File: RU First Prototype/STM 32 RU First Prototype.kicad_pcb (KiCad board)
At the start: 4 copper layers, 91 parts, among them J1 Conn_01x02, J10 Conn_01x02_Pin, J11 Conn_01x02_Pin, J12 1776113-2, J2 USB_C_Receptacle, J3 Conn_01x02_Pin, J4 Conn_01x04, J5 Conn_01x02_Pin, J7 1776113-2, J9 Conn_01x02_Pin, Q1 SISA96DN-T1, Q3 SISA96DN-T1, SW1 SW_SPDT, U1 STM32F412RGTx, U2 AMS1117-3.3, U3 MS5611, U4 KX134-1211, U5 W25Q16JVSS, U6 TCAN330, U7 TCAN330, Y1 Crystal_8Mhz

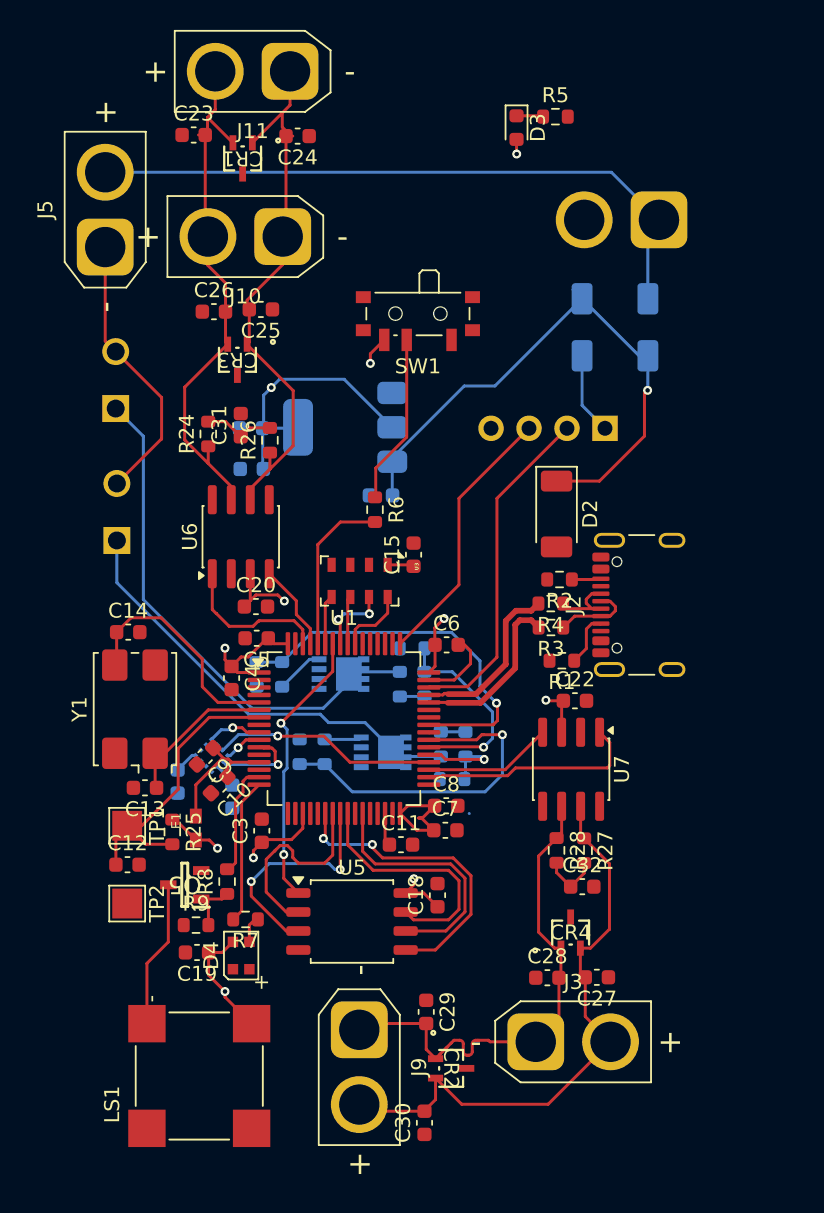
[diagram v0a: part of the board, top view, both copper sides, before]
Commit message: Edge cuts to start
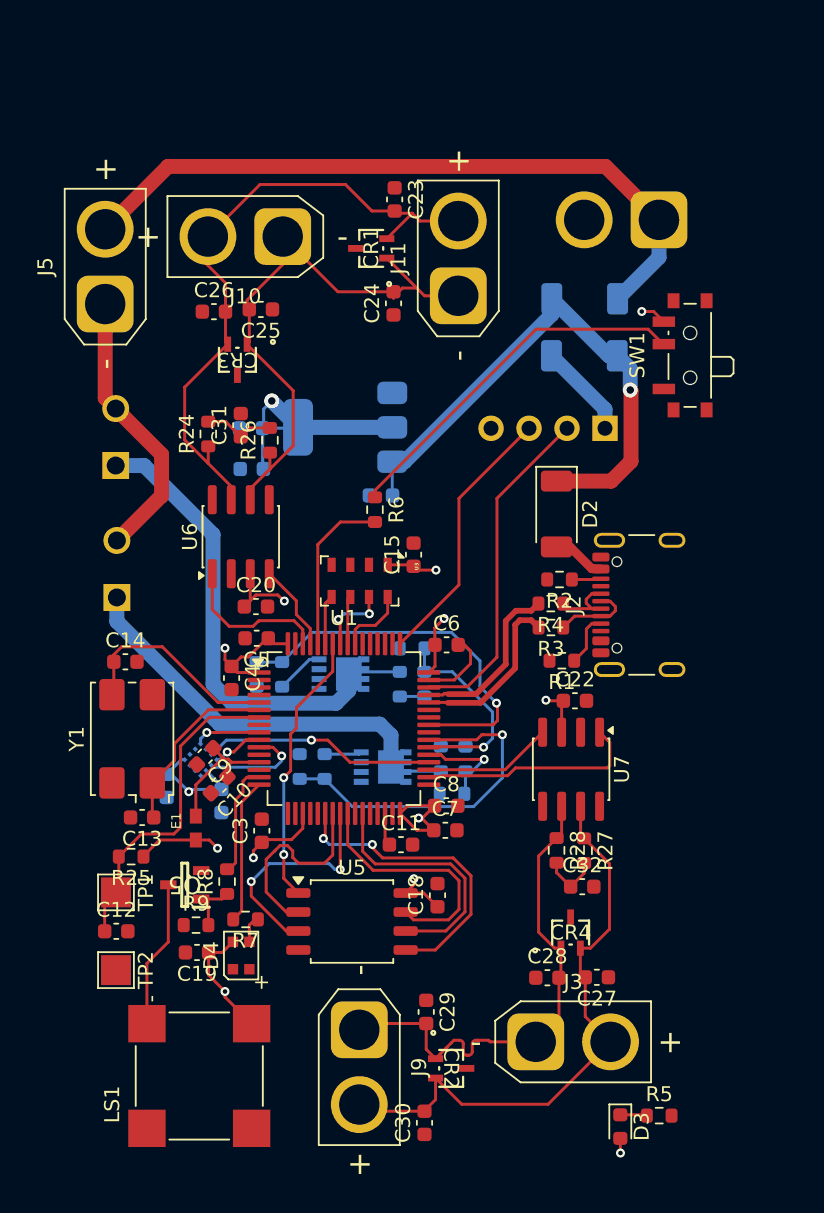
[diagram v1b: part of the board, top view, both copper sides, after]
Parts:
- moved R5 67.2 mm to (142.5, 125.7)
- moved D3 67.2 mm to (139.9, 126.4)
- moved J11 18.8 mm to (129.0, 70.9), turned to 90 degrees
- moved SW1 18.0 mm to (144.2, 74.8), turned to 90 degrees
- moved C23 14.1 mm to (124.8, 64.4), turned to -90 degrees
- moved C24 12.9 mm to (124.7, 71.4), turned to 90 degrees
- moved CR1 10.5 mm to (123.2, 67.7), turned to 90 degrees
- moved C12 4.52 mm to (106.2, 113.4)
- moved TP1 4.52 mm to (106.1, 110.8)
- moved TP2 4.52 mm to (106.1, 116.0)
- moved J12 3.81 mm to (106.1, 80.3)
- moved J5 3.81 mm to (105.4, 71.4)
- moved J7 3.81 mm to (106.2, 89.1)
- moved R25 3.21 mm to (107.1, 108.4), turned to 180 degrees
- moved D5 2.05 mm to (137.4, 74.9)
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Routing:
- net Net-(SW1-B): track 11.4 -> 24.7 mm
- net /CAN_H: track 35.9 -> 43.7 mm
- net +3V3: track 75.4 -> 81.1 mm, vias 11 -> 14
- net /V_2S: track 43.9 -> 47.7 mm
- net /V_USB: track 0.42 -> 4.00 mm
- net /CAN_L: track 36.8 -> 39.2 mm
- net /OSC_OUT: track 10.5 -> 12.8 mm
- net /V_IN: track 39.9 -> 38.0 mm
- net /NRST: track 20.0 -> 22.0 mm
- net /V_MAIN: track 35.0 -> 33.5 mm
- net /OSC_IN: track 15.6 -> 14.2 mm
- net /KX_SDI: track 6.12 -> 7.34 mm
- net /KX_SDO: track 2.54 -> 3.39 mm
- net /SW_VCC: track 5.48 -> 6.33 mm
- net /KX_CS: track 3.64 -> 4.43 mm
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
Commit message: Added fill zones and all
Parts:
- added REF**: MountingHole_3.2mm_M3, MountingHole:MountingHole_3.2mm_M3, F.Cu at (151.2, 61.7)
- added REF**: MountingHole_3.2mm_M3, MountingHole:MountingHole_3.2mm_M3, F.Cu at (98.8, 61.6)
- added REF**: MountingHole_3.2mm_M3, MountingHole:MountingHole_3.2mm_M3, F.Cu at (98.7, 127.4)
- added REF**: MountingHole_3.2mm_M3, MountingHole:MountingHole_3.2mm_M3, F.Cu at (151.2, 127.4)
- moved R20 2.92 mm to (128.4, 96.0), turned to 90 degrees
- moved R11 1.73 mm to (115.5, 94.5), turned to -90 degrees
- moved R14 1.72 mm to (118.4, 104.0), turned to 90 degrees
- moved C22 1.54 mm to (135.3, 97.9)
- moved C12 1.28 mm to (107.4, 113.2)
- moved R2 1.20 mm to (134.6, 89.7)
- moved R19 1.08 mm to (126.8, 97.9)
- moved C5 1.07 mm to (114.5, 94.0)
- moved C10 1.05 mm to (113.6, 104.5), turned to -90 degrees
- moved C4 0.99 mm to (112.9, 96.4), turned to 135 degrees
- moved U5 0.94 mm to (121.9, 113.6)
- moved R23 0.83 mm to (128.1, 104.8)
- moved C32 0.82 mm to (136.5, 110.5)
- moved C13 0.79 mm to (107.1, 105.6)
- moved R18 0.77 mm to (125.1, 97.6)
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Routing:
- net GND: track 6.88 -> 19.4 mm, vias 0 -> 40
- net /V_USB: track 4.00 -> 12.0 mm
- net +3V3: track 81.1 -> 76.5 mm
- net /Main: track 26.0 -> 29.4 mm
- net /PC7: track 13.5 -> 10.6 mm
- net /ALT_CS: track 3.30 -> 5.45 mm
- net /FLASH_IO0: track 20.7 -> 22.3 mm
- net /FLASH_CLK: track 16.9 -> 18.5 mm
- net Net-(J2-CC2): track 1.96 -> 3.23 mm
- net /FLASH_CS: track 18.4 -> 19.7 mm
- net /FLASH_IO3: track 16.5 -> 17.7 mm
- net /FLASH_IO2: track 15.5 -> 16.5 mm
- net /PC6: track 6.91 -> 7.87 mm
- net /FLASH_IO1: track 13.6 -> 14.5 mm
- net /OSC_IN: track 14.2 -> 15.0 mm
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- added copper zone on In2.Cu, net +3V3
- added copper zone on B.Cu, net GND
- added copper zone on F.Cu, net GND
- added copper zone on In1.Cu, net GND
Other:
- board outline added: 60.8 x 74.2 mm

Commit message: Made some changes
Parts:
- added G***: LOGO, RT_Graphics:RT_logo, F.Cu at (133.0, 59.0)
- added G***: LOGO, RT_Graphics:Ember_logo, F.Cu at (121.5, 76.5)
- added REF**: KiCad-Logo2_5mm_SilkScreen, Symbol:KiCad-Logo2_5mm_SilkScreen, F.Cu at (115.5, 58.0)
- moved REF** 9.42 mm to (143.0, 132.0)
- moved REF** 9.20 mm to (143.0, 57.5)
- moved R5 8.82 mm to (135.8, 131.5)
- moved REF** 7.81 mm to (105.0, 132.0)
- moved REF** 7.41 mm to (105.0, 57.5)
- moved D3 4.82 mm to (135.8, 129.0), turned to 0 degrees
- moved R11 1.81 mm to (115.0, 96.2)
- moved R14 1.73 mm to (118.5, 102.3), turned to -90 degrees
- moved C17 1.71 mm to (108.5, 105.0)
- moved R20 1.67 mm to (128.4, 97.7), turned to -90 degrees
- moved C16 0.90 mm to (114.0, 105.0)
- moved R22 0.82 mm to (129.0, 102.5)
- moved C1 0.79 mm to (123.8, 85.0)
- moved R21 0.75 mm to (127.4, 102.4)
- moved R19 0.28 mm to (126.7, 97.6)
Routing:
- net /V_2S: track 47.7 -> 52.2 mm
- net +3V3: track 76.5 -> 79.8 mm, vias 14 -> 19
- net /Main: track 29.4 -> 31.4 mm
- net /V_IN: track 38.0 -> 39.8 mm
- net GND: track 19.4 -> 20.8 mm, vias 40 -> 44
- net /V_DROGUE: track 28.5 -> 27.3 mm
- net Net-(D3-K): track 1.80 -> 2.50 mm
- net /SW_VCC: track 6.33 -> 6.87 mm
- added copper zone on B.Cu, net +3V3
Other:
- board size 60.8 x 74.2 mm -> 45 x 81.5 mm
- board text added: "Aug 2026"
- board text added: "EMBER"
- board text added: "RU V1 R1"

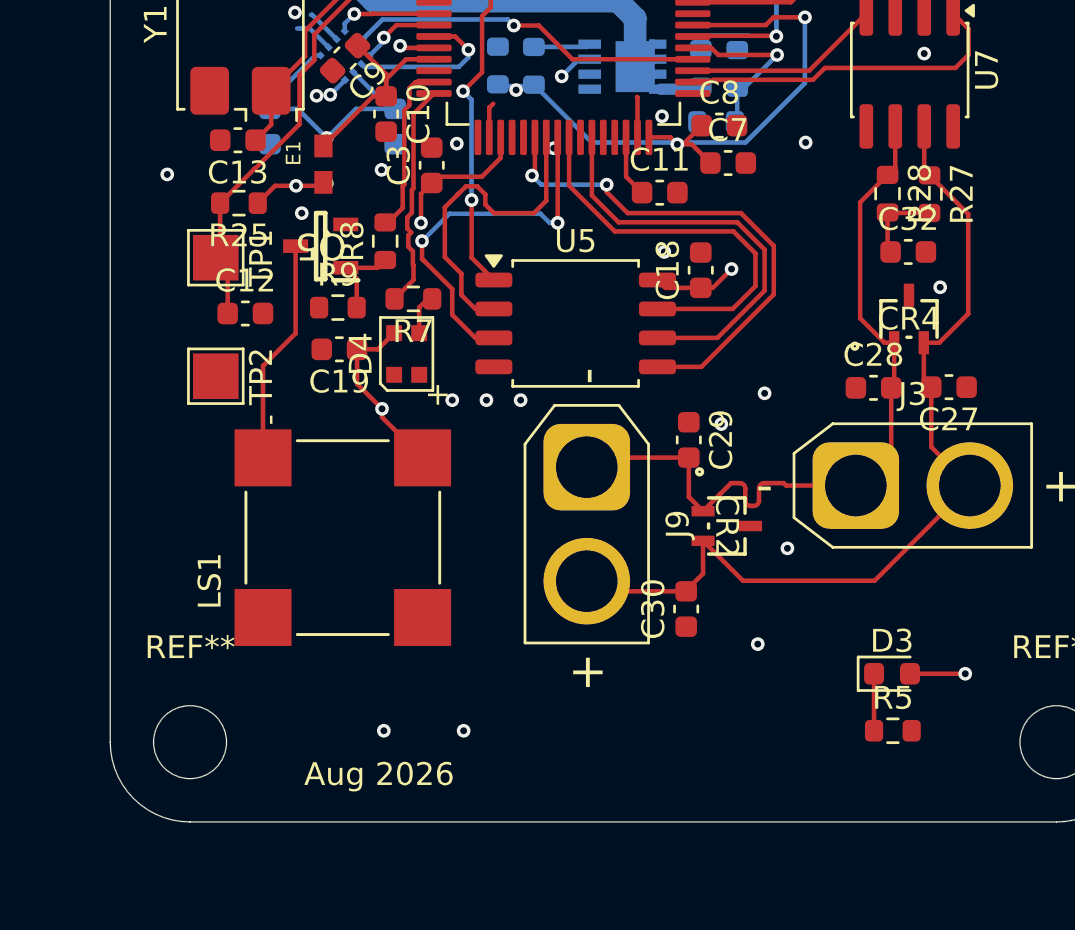
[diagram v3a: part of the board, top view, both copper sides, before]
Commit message: made some changes to routings
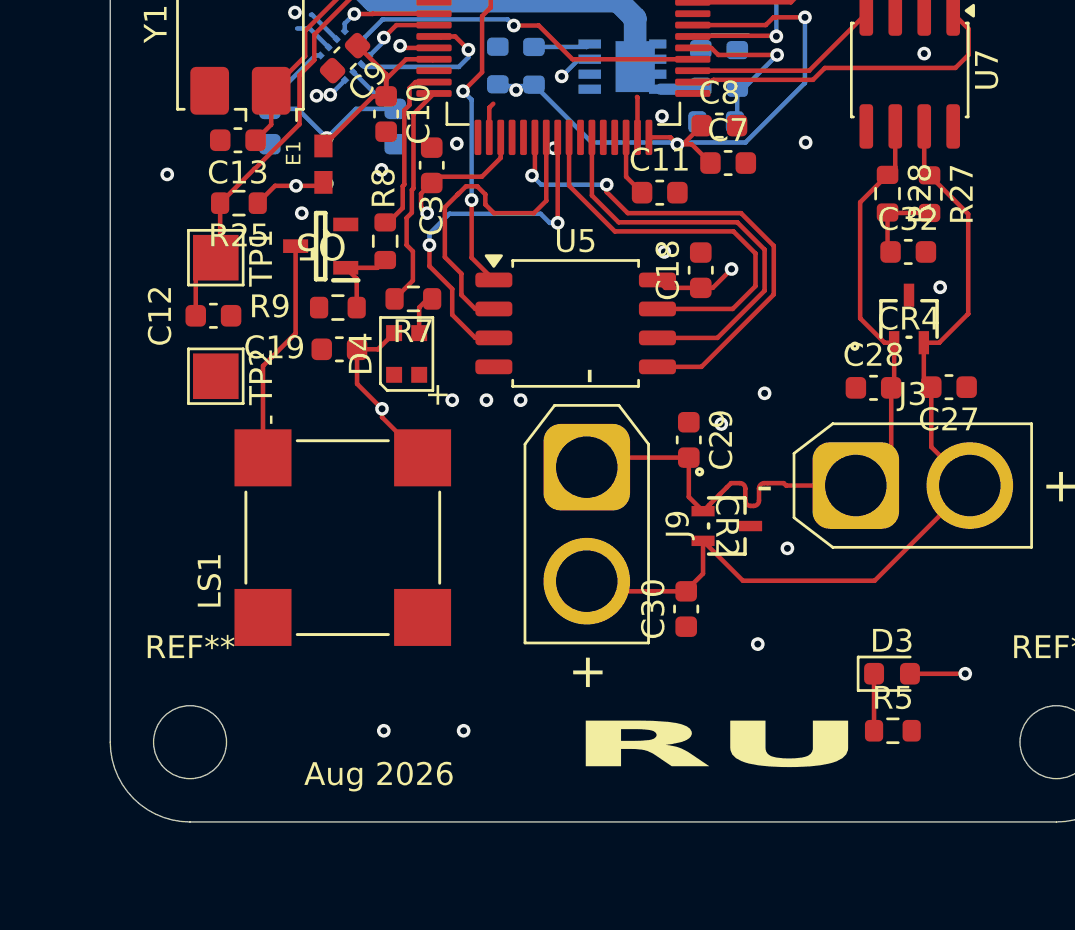
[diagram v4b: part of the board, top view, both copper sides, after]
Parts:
- moved C12 1.40 mm to (106.0, 113.3)
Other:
- board text added: "RU"
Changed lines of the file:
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@@
 		(tags "resistor")
 		(property "Reference" "R9"
-			(at 0 -1.43 0)
+			(at -2.985 -0.04 0)
 			(layer "F.SilkS")
 			(effects
@@
 		(tags "capacitor")
 		(property "Reference" "C19"
-			(at 0 -1.43 0)
+			(at 2.85 0.07 0)
 			(layer "F.SilkS")
 			(effects
@@
 		)
 		(property "Value" "STM32F412RGTx"
-			(at -8.595 7.545 0)
+			(at 0 0 0)
 			(layer "F.Fab")
 			(effects
@@
 	(footprint "Capacitor_SMD:C_0603_1608Metric"
 		(layer "F.Cu")
-		(at 107.425 113.2)
+		(at 106.025 113.3)
 		(descr "Capacitor SMD 0603 (1608 Metric), square (rectangular) end terminal, IPC-7351 nominal, (Body size source: IPC-SM-782 page 76, https://www.pcb-3d.com/wordpress/wp-content/uploads/ipc-sm-782a_amendment_1_and_2.pdf), generated with kicad-footprint-generator")
 		(tags "capacitor")
 		(property "Reference" "C12"
-			(at 0 -1.43 0)
+			(at -2.325 0 90)
 			(layer "F.SilkS")
 			(effects
@@
 		(tags "capacitor")
 		(property "Reference" "C3"
-			(at 0 -1.43 90)
+			(at -2.2 0 90)
 			(layer "F.SilkS")
 			(effects
@@
 		(tags "resistor")
 		(property "Reference" "R8"
-			(at 0 -1.43 90)
+			(at 2.33 -0.06 90)
 			(layer "F.SilkS")
 			(effects
@@
 		)
 	)
+	(gr_text "RU"
+		(at 121.6 133.3 0)
+		(layer "F.SilkS")
+		(effects
+			(font
+				(face "OCR A Extended")
+				(size 2 6)
+				(thickness 0.5)
+				(bold yes)
+			)
+			(justify left bottom)
+		)
+		(render_cache "RU" 0
+			(polygon
+				(pts
+					(xy 125.175013 131.150416) (xy 125.417517 131.184286) (xy 125.638799 131.241995) (xy 125.81162 131.315835)
+					(xy 125.913162 131.396908) (xy 125.947644 131.487948) (xy 125.947644 131.618374) (xy 125.913187 131.71032)
+					(xy 125.81207 131.791612) (xy 125.640631 131.865059) (xy 125.420782 131.92223) (xy 125.177746 131.955922)
+					(xy 124.90314 131.967397) (xy 124.485118 131.967397) (xy 125.884263 132.769612) (xy 125.93548 132.806879)
+					(xy 125.951674 132.842763) (xy 125.924444 132.887235) (xy 125.841399 132.925439) (xy 125.722749 132.951529)
+					(xy 125.591538 132.96) (xy 125.461472 132.953089) (xy 125.356398 132.932565) (xy 125.26987 132.896741)
+					(xy 123.65457 131.967397) (xy 123.176831 131.967397) (xy 123.176831 132.841053) (xy 123.149855 132.886968)
+					(xy 123.068754 132.925439) (xy 122.950499 132.951386) (xy 122.812665 132.96) (xy 122.675206 132.951337)
+					(xy 122.56024 132.925439) (xy 122.482542 132.887235) (xy 122.456559 132.841542) (xy 122.456559 131.732923)
+					(xy 123.168771 131.732923) (xy 124.902773 131.732923) (xy 125.031406 131.724912) (xy 125.138346 131.70105)
+					(xy 125.211121 131.665636) (xy 125.235432 131.623258) (xy 125.235432 131.490879) (xy 125.211109 131.448523)
+					(xy 125.138346 131.41321) (xy 125.031378 131.389252) (xy 124.902773 131.381214) (xy 123.168771 131.381214)
+					(xy 123.168771 131.732923) (xy 122.456559 131.732923) (xy 122.456559 131.138925) (xy 124.90314 131.138925)
+				)
+			)
+			(polygon
+				(pts
+					(xy 127.510554 132.61232) (xy 127.510554 131.260191) (xy 127.536886 131.214324) (xy 127.616434 131.174951)
+					(xy 127.732943 131.147812) (xy 127.86666 131.138925) (xy 128.000484 131.147659) (xy 128.116521 131.174218)
+					(xy 128.196491 131.212788) (xy 128.222766 131.25726) (xy 128.222766 132.609877) (xy 128.247102 132.65015)
+					(xy 128.321685 132.685471) (xy 128.429967 132.709704) (xy 128.555425 132.717711) (xy 129.965195 132.717711)
+					(xy 130.093914 132.70978) (xy 130.200767 132.686203) (xy 130.273631 132.65133) (xy 130.297854 132.609877)
+					(xy 130.297854 131.259947) (xy 130.323941 131.213098) (xy 130.401535 131.174218) (xy 130.516672 131.147747)
+					(xy 130.65396 131.138925) (xy 130.790869 131.147745) (xy 130.905652 131.174218) (xy 130.983527 131.213225)
+					(xy 131.009699 131.260191) (xy 131.009699 132.609511) (xy 130.975198 132.70097) (xy 130.873626 132.782409)
+					(xy 130.700854 132.856563) (xy 130.479494 132.914493) (xy 130.236996 132.948474) (xy 129.965195 132.96)
+					(xy 128.555059 132.96) (xy 128.280392 132.948551) (xy 128.037225 132.914935) (xy 127.817201 132.857906)
+					(xy 127.645869 132.784636) (xy 127.544922 132.703702)
+				)
+			)
+		)
+	)
 	(segment
 		(start 118.125 104.175)
@@
 	)
 	(segment
-		(start 115.13 109.226264)
-		(end 115.13 107.945)
+		(start 116.4 91.1)
+		(end 115.11 89.81)
 		(width 0.2)
 		(layer "F.Cu")
@@
 	)
 	(segment
-		(start 116.4 91.1)
-		(end 115.11 89.81)
+		(start 133.76 97.2)
+		(end 134.5 97.94)
 		(width 0.2)
 		(layer "F.Cu")
@@
 	)
 	(segment
-		(start 133.76 97.2)
-		(end 134.5 97.94)
+		(start 115.13 108.53)
+		(end 115.13 107.945)
 		(width 0.2)
 		(layer "F.Cu")
@@
 	)
 	(segment
-		(start 115.13 107.945)
-		(end 115.6 107.475)
-		(width 0.2)
-		(layer "F.Cu")
-		(net "+3V3")
-	)
-	(segment
 		(start 115.875 107.2)
 		(end 117.8 107.2)
@@
 	)
 	(segment
+		(start 115.13 107.945)
+		(end 115.6 107.475)
+		(width 0.2)
+		(layer "F.Cu")
+		(net "+3V3")
+	)
+	(segment
 		(start 127.005 105.78)
 		(end 127.825 106.6)
@@
 	)
 	(segment
+		(start 115.4 108.8)
+		(end 115.13 108.53)
+		(width 0.2)
+		(layer "F.Cu")
+		(net "+3V3")
+	)
+	(segment
 		(start 112.325 116.285)
 		(end 112.325 114.77)
@@
 	)
 	(via blind
-		(at 115.13 109.226264)
+		(at 115.4 108.8)
 		(size 0.6)
 		(drill 0.3)
@@
 	)
 	(segment
-		(start 109.8 104.90011)
-		(end 107.851111 106.848999)
+		(start 105.25 113.3)
+		(end 105.25 111.6325)
 		(width 0.2)
 		(layer "F.Cu")
@@
 	)
 	(segment
-		(start 109.8 102.7371)
-		(end 109.8 104.90011)
+		(start 109.8 104.90011)
+		(end 107.851111 106.848999)
 		(width 0.2)
 		(layer "F.Cu")
@@
 	)
 	(segment
-		(start 106.65 111.2725)
+		(start 105.25 111.6325)
 		(end 106.13 110.7525)
 		(width 0.2)
@@
 	)
 	(segment
-		(start 115.7 99.05)
-		(end 112.3671 99.05)
+		(start 109.8 102.7371)
+		(end 109.8 104.90011)
 		(width 0.2)
 		(layer "F.Cu")
@@
 	)
 	(segment
-		(start 106.32 108.36)
-		(end 106.32 110.5625)
+		(start 106.65 111.2725)
+		(end 106.13 110.7525)
 		(width 0.2)
 		(layer "F.Cu")
@@
 	)
 	(segment
-		(start 105.375 111.5075)
-		(end 106.13 110.7525)
+		(start 115.7 99.05)
+		(end 112.3671 99.05)
 		(width 0.2)
 		(layer "F.Cu")
@@
 	)
 	(segment
-		(start 106.65 113.2)
-		(end 106.65 111.2725)
+		(start 106.32 108.36)
+		(end 106.32 110.5625)
 		(width 0.2)
 		(layer "F.Cu")
@@
 	)
 	(segment
-		(start 114.8 107.7079)
-		(end 114.729 107.7789)
-		(width 0.2)
-		(layer "F.Cu")
-		(net "/mLED")
-	)
-	(segment
-		(start 114.774 110.473943)
-		(end 114.774 111.05235)
+		(start 114.729 108.777321)
+		(end 114.5 109.006321)
 		(width 0.2)
 		(layer "F.Cu")
@@
 	)
 	(segment
-		(start 114.729 108.777321)
-		(end 114.529 108.977321)
+		(start 114.8 107.7079)
+		(end 114.729 107.7789)
 		(width 0.2)
 		(layer "F.Cu")
@@
 	)
 	(segment
-		(start 114.574 109.776057)
-		(end 114.574 110.273943)
-		(width 0.2)
-		(layer "F.Cu")
-		(net "/mLED")
-	)
-	(segment
-		(start 114.574 110.273943)
-		(end 114.774 110.473943)
+		(start 114.5 109.006321)
+		(end 114.5 110.199943)
 		(width 0.2)
 		(layer "F.Cu")
@@
 	)
 	(segment
-		(start 114.8 111.07835)
-		(end 114.8 111.73)
-		(width 0.2)
-		(layer "F.Cu")
-		(net "/mLED")
-	)
-	(segment
-		(start 114.774 111.05235)
-		(end 114.8 111.07835)
+		(start 114.775 111.755)
+		(end 113.97 112.56)
 		(width 0.2)
 		(layer "F.Cu")
@@
 	)
 	(segment
-		(start 114.529 109.475207)
-		(end 114.701925 109.648132)
+		(start 114.5 110.199943)
+		(end 114.775 110.474943)
 		(width 0.2)
 		(layer "F.Cu")
@@
 	)
 	(segment
-		(start 114.8 111.73)
-		(end 113.97 112.56)
+		(start 114.775 110.474943)
+		(end 114.775 111.755)
 		(width 0.2)
 		(layer "F.Cu")
@@
 	)
 	(segment
-		(start 114.529 108.977321)
-		(end 114.529 109.475207)
-		(width 0.2)
-		(layer "F.Cu")
-		(net "/mLED")
-	)
-	(segment
 		(start 115.7 103.55)
 		(end 114.8 104.45)
@@
 	)
 	(segment
-		(start 114.701925 109.648132)
-		(end 114.574 109.776057)
-		(width 0.2)
-		(layer "F.Cu")
-		(net "/mLED")
-	)
-	(segment
 		(start 120 107.15)
 		(end 120.125 107.025)
@@
 	)
 	(segment
-		(start 117.512501 114.27)
-		(end 118.325 114.27)
+		(start 115.5 111.125)
+		(end 115.5 110.2)
 		(width 0.2)
 		(layer "F.Cu")
@@
 	)
 	(segment
-		(start 115.175 110.8)
-		(end 115.280625 110.905625)
+		(start 117.512501 114.27)
+		(end 118.325 114.27)
 		(width 0.2)
 		(layer "F.Cu")
@@
 	)
 	(segment
-		(start 115.175 110.8)
-		(end 116.5 112.125)
+		(start 115.5 110.2)
+		(end 115.4 110.3)
 		(width 0.2)
 		(layer "F.Cu")
@@
 	)
 	(segment
-		(start 115.175 110.025)
-		(end 115.175 110.8)
+		(start 121.125 109.225)
+		(end 121.125 105.475)
 		(width 0.2)
 		(layer "F.Cu")
@@
 	)
 	(segment
-		(start 121.125 109.225)
-		(end 121.125 105.475)
+		(start 116.5 112.125)
+		(end 116.5 113.257499)
 		(width 0.2)
 		(layer "F.Cu")
@@
 	(segment
 		(start 116.5 112.125)
-		(end 116.5 113.257499)
+		(end 115.5 111.125)
 		(width 0.2)
 		(layer "F.Cu")
@@
 	)
 	(via
-		(at 115.175 110.025)
+		(at 115.5 110.2)
 		(size 0.6)
 		(drill 0.3)
@@
 	(segment
 		(start 120.375 108.825)
-		(end 116.375 108.825)
+		(end 120.775 109.225)
 		(width 0.2)
 		(layer "B.Cu")
@@
 	)
 	(segment
-		(start 116.375 108.825)
-		(end 115.175 110.025)
+		(start 115.5 109.7)
+		(end 116.375 108.825)
 		(width 0.2)
 		(layer "B.Cu")
@@
 	)
 	(segment
-		(start 121.125 109.225)
-		(end 120.775 109.225)
+		(start 115.5 110.2)
+		(end 115.5 109.7)
 		(width 0.2)
 		(layer "B.Cu")
@@
 	(segment
 		(start 120.775 109.225)
+		(end 121.125 109.225)
+		(width 0.2)
+		(layer "B.Cu")
+		(net "/FLASH_IO2")
+	)
+	(segment
+		(start 116.375 108.825)
 		(end 120.375 108.825)
 		(width 0.2)
